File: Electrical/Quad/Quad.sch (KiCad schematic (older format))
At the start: 4 parts, among them J101 01x04, J102 01x04, J103 01x03, J104 01x03

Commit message: Fixed DRC errors
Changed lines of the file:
@@
 $EndComp
 $Comp
-L GND #PWR104
+L GND #PWR01
 U 1 1 5A59574B
 P 9700 1250
-F 0 "#PWR104" H 9700 1000 50  0001 C CNN
+F 0 "#PWR01" H 9700 1000 50  0001 C CNN
 F 1 "GND" H 9700 1100 50  0000 C CNN
 F 2 "" H 9700 1250 50  0001 C CNN
@@
 $EndComp
 $Comp
-L +5V #PWR102
+L +5V #PWR02
 U 1 1 5A595753
 P 9650 1000
-F 0 "#PWR102" H 9650 850 50  0001 C CNN
+F 0 "#PWR02" H 9650 850 50  0001 C CNN
 F 1 "+5V" H 9650 1140 50  0000 C CNN
 F 2 "" H 9650 1000 50  0001 C CNN
@@
 $EndComp
 $Comp
-L GND #PWR105
+L GND #PWR03
 U 1 1 5A59801B
 P 9700 4150
-F 0 "#PWR105" H 9700 3900 50  0001 C CNN
+F 0 "#PWR03" H 9700 3900 50  0001 C CNN
 F 1 "GND" H 9700 4000 50  0000 C CNN
 F 2 "" H 9700 4150 50  0001 C CNN
@@
 $EndComp
 $Comp
-L +5V #PWR103
+L +5V #PWR04
 U 1 1 5A598022
 P 9650 3900
-F 0 "#PWR103" H 9650 3750 50  0001 C CNN
+F 0 "#PWR04" H 9650 3750 50  0001 C CNN
 F 1 "+5V" H 9650 4040 50  0000 C CNN
 F 2 "" H 9650 3900 50  0001 C CNN
@@
 	9700 3900 9650 3900
 $Comp
-L GND #PWR101
+L GND #PWR05
 U 1 1 5A599898
 P 3000 1700
-F 0 "#PWR101" H 3000 1450 50  0001 C CNN
+F 0 "#PWR05" H 3000 1450 50  0001 C CNN
 F 1 "GND" H 3000 1550 50  0000 C CNN
 F 2 "" H 3000 1700 50  0001 C CNN
@@
 	2400 1300 3000 1300
 Wire Wire Line
-	3000 1300 3000 1400
-Wire Wire Line
-	3000 1400 3000 1500
-Wire Wire Line
-	3000 1500 3000 1600
-Wire Wire Line
-	3000 1600 3000 1700
+	3000 1300 3000 1700
 Wire Wire Line
 	2400 1400 3000 1400

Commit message: Added footprints for Quad
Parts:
- J101, J102: footprint (none) -> Pin_Headers:Pin_Header_Straight_1x04_Pitch2.54mm_SMD_Pin1Right
- J103, J104: footprint (none) -> Pin_Headers:Pin_Header_Straight_1x03_Pitch2.54mm_SMD_Pin1Right
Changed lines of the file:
@@
 F 0 "J101" H 9550 2100 50  0000 C CNN
 F 1 "01x04" V 9650 1850 50  0000 C CNN
-F 2 "" H 9550 1900 50  0001 C CNN
+F 2 "Pin_Headers:Pin_Header_Straight_1x04_Pitch2.54mm_SMD_Pin1Right" H 9550 1900 50  0001 C CNN
 F 3 "" H 9550 1900 50  0001 C CNN
 	1    9550 1900
@@
 F 0 "J103" H 9900 1300 50  0000 C CNN
 F 1 "01x03" V 10000 1100 50  0000 C CNN
-F 2 "" H 9900 1100 50  0001 C CNN
+F 2 "Pin_Headers:Pin_Header_Straight_1x03_Pitch2.54mm_SMD_Pin1Right" H 9900 1100 50  0001 C CNN
 F 3 "" H 9900 1100 50  0001 C CNN
 	1    9900 1100
@@
 F 0 "J102" H 9550 5000 50  0000 C CNN
 F 1 "01x04" V 9650 4750 50  0000 C CNN
-F 2 "" H 9550 4800 50  0001 C CNN
+F 2 "Pin_Headers:Pin_Header_Straight_1x04_Pitch2.54mm_SMD_Pin1Right" H 9550 4800 50  0001 C CNN
 F 3 "" H 9550 4800 50  0001 C CNN
 	1    9550 4800
@@
 F 0 "J104" H 9900 4200 50  0000 C CNN
 F 1 "01x03" V 10000 4000 50  0000 C CNN
-F 2 "" H 9900 4000 50  0001 C CNN
+F 2 "Pin_Headers:Pin_Header_Straight_1x03_Pitch2.54mm_SMD_Pin1Right" H 9900 4000 50  0001 C CNN
 F 3 "" H 9900 4000 50  0001 C CNN
 	1    9900 4000

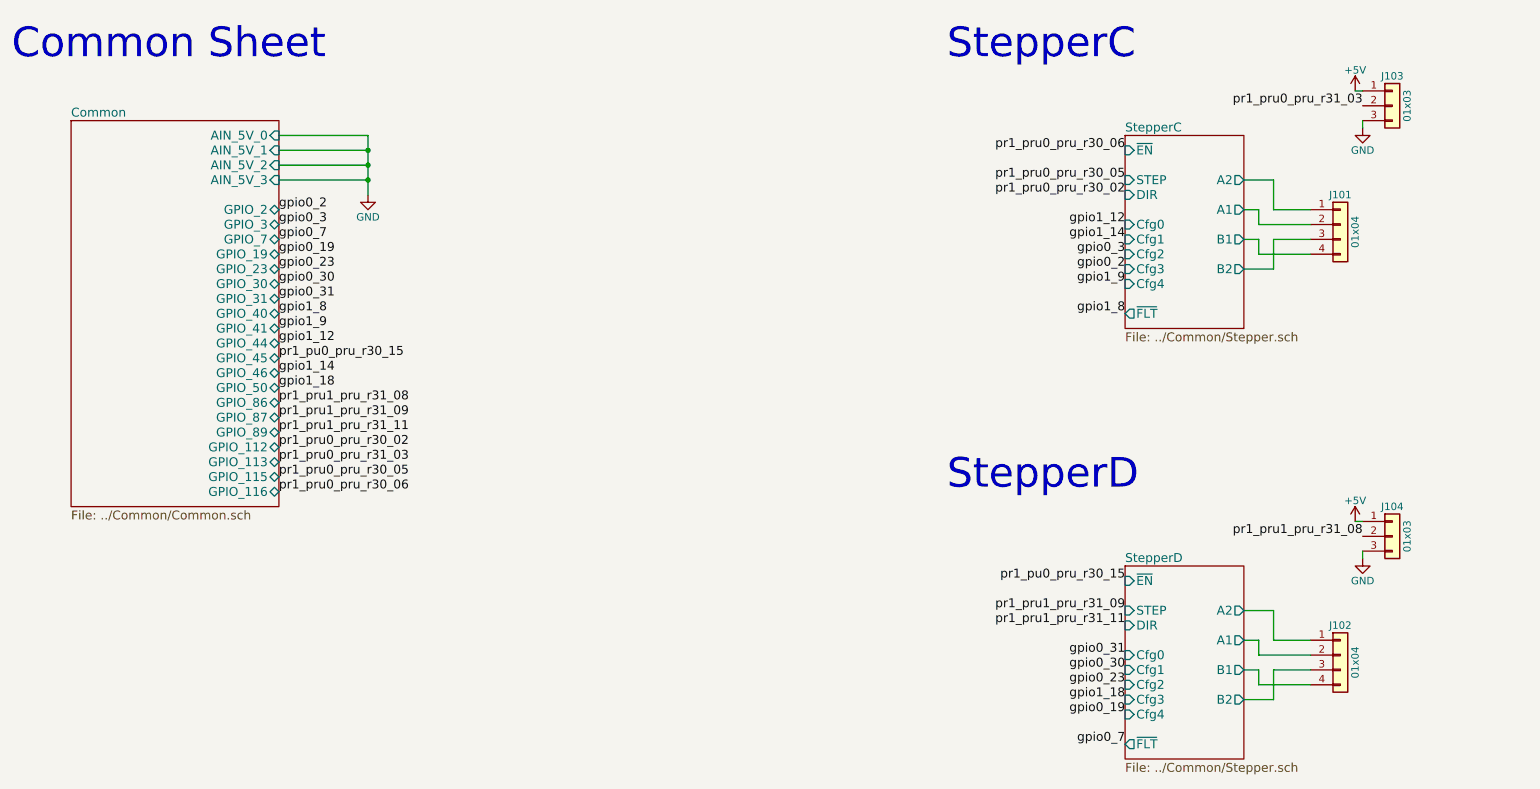
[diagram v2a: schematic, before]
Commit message: Completed Quad stepper version of the board.
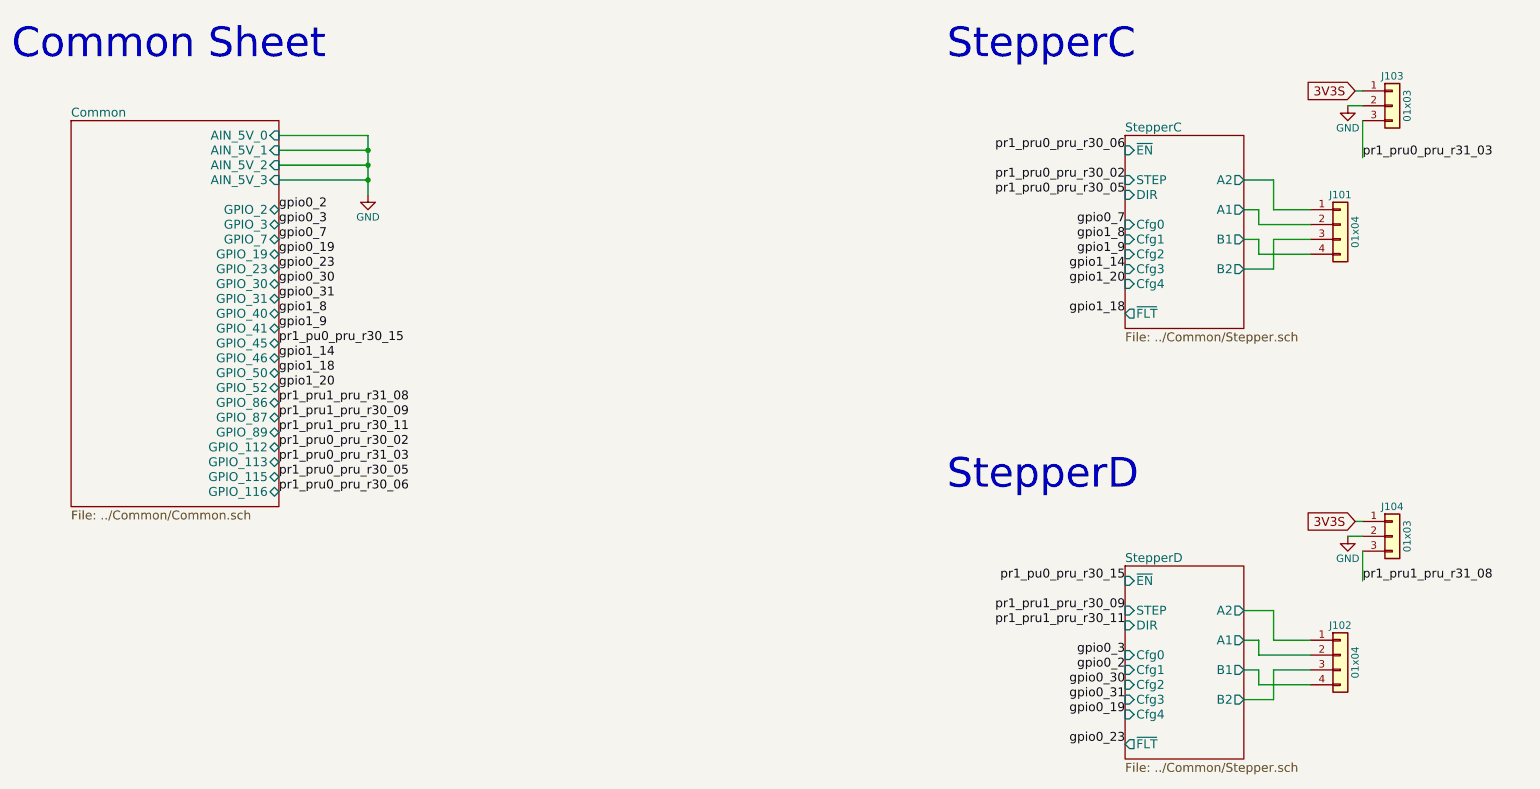
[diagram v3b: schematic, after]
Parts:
- J101, J102: footprint Pin_Headers:Pin_Header_Straight_1x04_Pitch2.54mm_SMD_Pin1Right -> footprints:Molex-SL-4POS
- J103, J104: footprint Pin_Headers:Pin_Header_Straight_1x03_Pitch2.54mm_SMD_Pin1Right -> Connectors_JST:JST_XH_B03B-XH-A_03x2.50mm_Straight
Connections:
- net GND: now also J103.2 (Pin_2), J104.2 (Pin_2); no longer J103.3 (Pin_3), J104.3 (Pin_3)
- net pr1_pru0_pru_r31_03: now also J103.3 (Pin_3); no longer J103.2 (Pin_2)
- net pr1_pru1_pru_r31_08: now also J104.3 (Pin_3); no longer J104.2 (Pin_2)
- net +5V renamed 3V3S
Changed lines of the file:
@@
 LIBS:dc-dc
 LIBS:allegro
+LIBS:mechanical
 LIBS:Quad-cache
 EELAYER 25 0
@@
 F13 "GPIO_40" T R 2400 2500 60
 F14 "GPIO_41" T R 2400 2600 60
-F15 "GPIO_44" T R 2400 2700 60
-F16 "GPIO_45" T R 2400 2800 60
-F17 "GPIO_46" T R 2400 2900 60
-F18 "GPIO_50" T R 2400 3000 60
-F19 "GPIO_86" T R 2400 3100 60
-F20 "GPIO_87" T R 2400 3200 60
-F21 "GPIO_112" T R 2400 3400 60
-F22 "GPIO_113" T R 2400 3500 60
-F23 "GPIO_115" T R 2400 3600 60
-F24 "GPIO_116" T R 2400 3700 60
-F25 "GPIO_89" T R 2400 3300 60
+F15 "GPIO_45" T R 2400 2700 60
+F16 "GPIO_46" T R 2400 2800 60
+F17 "GPIO_50" T R 2400 2900 60
+F18 "GPIO_86" T R 2400 3100 60
+F19 "GPIO_87" T R 2400 3200 60
+F20 "GPIO_112" T R 2400 3400 60
+F21 "GPIO_113" T R 2400 3500 60
+F22 "GPIO_115" T R 2400 3600 60
+F23 "GPIO_116" T R 2400 3700 60
+F24 "GPIO_89" T R 2400 3300 60
+F25 "GPIO_52" T R 2400 3000 60
 $EndSheet
 Text Label 2400 1800 0    60   ~ 0
@@
 Text Label 2400 1900 0    60   ~ 0
 gpio0_3
-Text Label 2400 3000 0    60   ~ 0
+Text Label 2400 2900 0    60   ~ 0
 gpio1_18
 Text Label 2400 2200 0    60   ~ 0
@@
 gpio0_19
 Text Label 2400 2700 0    60   ~ 0
-gpio1_12
+pr1_pu0_pru_r30_15
 Text Label 2400 2800 0    60   ~ 0
-pr1_pu0_pru_r30_15
-Text Label 2400 2900 0    60   ~ 0
 gpio1_14
 Text Label 2400 3100 0    60   ~ 0
 pr1_pru1_pru_r31_08
 Text Label 2400 3200 0    60   ~ 0
-pr1_pru1_pru_r31_09
+pr1_pru1_pru_r30_09
 Text Label 2400 3300 0    60   ~ 0
-pr1_pru1_pru_r31_11
+pr1_pru1_pru_r30_11
 Text Label 2400 3400 0    60   ~ 0
 pr1_pru0_pru_r30_02
@@
 U 1 1 5A595731
 P 9550 1900
+AR Path="/5A595731" Ref="J101"  Part="1"
+AR Path="/5A579457/5A595731" Ref="J101"  Part="1"
 F 0 "J101" H 9550 2100 50  0000 C CNN
 F 1 "01x04" V 9650 1850 50  0000 C CNN
-F 2 "Pin_Headers:Pin_Header_Straight_1x04_Pitch2.54mm_SMD_Pin1Right" H 9550 1900 50  0001 C CNN
+F 2 "footprints:Molex-SL-4POS" H 9550 1900 50  0001 C CNN
 F 3 "" H 9550 1900 50  0001 C CNN
 	1    9550 1900
@@
 F 0 "J103" H 9900 1300 50  0000 C CNN
 F 1 "01x03" V 10000 1100 50  0000 C CNN
-F 2 "Pin_Headers:Pin_Header_Straight_1x03_Pitch2.54mm_SMD_Pin1Right" H 9900 1100 50  0001 C CNN
+F 2 "Connectors_JST:JST_XH_B03B-XH-A_03x2.50mm_Straight" H 9900 1100 50  0001 C CNN
 F 3 "" H 9900 1100 50  0001 C CNN
 	1    9900 1100
-	1    0    0    -1
-$EndComp
-$Comp
-L GND #PWR01
-U 1 1 5A59574B
-P 9700 1250
-F 0 "#PWR01" H 9700 1000 50  0001 C CNN
-F 1 "GND" H 9700 1100 50  0000 C CNN
-F 2 "" H 9700 1250 50  0001 C CNN
-F 3 "" H 9700 1250 50  0001 C CNN
-	1    9700 1250
-	-1   0    0    -1
-$EndComp
-$Comp
-L +5V #PWR02
-U 1 1 5A595753
-P 9650 1000
-F 0 "#PWR02" H 9650 850 50  0001 C CNN
-F 1 "+5V" H 9650 1140 50  0000 C CNN
-F 2 "" H 9650 1000 50  0001 C CNN
-F 3 "" H 9650 1000 50  0001 C CNN
-	1    9650 1000
 	1    0    0    -1
 $EndComp
@@
 F 0 "J102" H 9550 5000 50  0000 C CNN
 F 1 "01x04" V 9650 4750 50  0000 C CNN
-F 2 "Pin_Headers:Pin_Header_Straight_1x04_Pitch2.54mm_SMD_Pin1Right" H 9550 4800 50  0001 C CNN
+F 2 "footprints:Molex-SL-4POS" H 9550 4800 50  0001 C CNN
 F 3 "" H 9550 4800 50  0001 C CNN
 	1    9550 4800
@@
 F 0 "J104" H 9900 4200 50  0000 C CNN
 F 1 "01x03" V 10000 4000 50  0000 C CNN
-F 2 "Pin_Headers:Pin_Header_Straight_1x03_Pitch2.54mm_SMD_Pin1Right" H 9900 4000 50  0001 C CNN
+F 2 "Connectors_JST:JST_XH_B03B-XH-A_03x2.50mm_Straight" H 9900 4000 50  0001 C CNN
 F 3 "" H 9900 4000 50  0001 C CNN
 	1    9900 4000
@@
 $EndComp
 $Comp
-L GND #PWR03
+L GND #PWR01
 U 1 1 5A59801B
-P 9700 4150
-F 0 "#PWR03" H 9700 3900 50  0001 C CNN
-F 1 "GND" H 9700 4000 50  0000 C CNN
-F 2 "" H 9700 4150 50  0001 C CNN
-F 3 "" H 9700 4150 50  0001 C CNN
-	1    9700 4150
+P 9600 4000
+F 0 "#PWR01" H 9600 3750 50  0001 C CNN
+F 1 "GND" H 9600 3850 50  0000 C CNN
+F 2 "" H 9600 4000 50  0001 C CNN
+F 3 "" H 9600 4000 50  0001 C CNN
+	1    9600 4000
 	-1   0    0    -1
 $EndComp
-$Comp
-L +5V #PWR04
-U 1 1 5A598022
-P 9650 3900
-F 0 "#PWR04" H 9650 3750 50  0001 C CNN
-F 1 "+5V" H 9650 4040 50  0000 C CNN
-F 2 "" H 9650 3900 50  0001 C CNN
-F 3 "" H 9650 3900 50  0001 C CNN
-	1    9650 3900
-	1    0    0    -1
-$EndComp
 Wire Wire Line
 	8900 1600 9100 1600
@@
 	9100 2000 9350 2000
 Wire Wire Line
-	9700 1250 9700 1200
-Wire Wire Line
 	9700 1000 9650 1000
 Wire Wire Line
@@
 	9100 4900 9350 4900
 Wire Wire Line
-	9700 4150 9700 4100
-Wire Wire Line
 	9700 3900 9650 3900
 $Comp
-L GND #PWR05
+L GND #PWR02
 U 1 1 5A599898
 P 3000 1700
-F 0 "#PWR05" H 3000 1450 50  0001 C CNN
+F 0 "#PWR02" H 3000 1450 50  0001 C CNN
 F 1 "GND" H 3000 1550 50  0000 C CNN
 F 2 "" H 3000 1700 50  0001 C CNN
@@
 	2400 1600 3000 1600
 Connection ~ 3000 1600
+Text Label 8100 1600 2    60   ~ 0
+pr1_pru0_pru_r30_02
 Text Label 8100 1700 2    60   ~ 0
-pr1_pru0_pru_r30_02
-Text Label 8100 1600 2    60   ~ 0
 pr1_pru0_pru_r30_05
+Text Label 8100 4900 2    60   ~ 0
+gpio0_2
+Text Label 8100 4800 2    60   ~ 0
+gpio0_3
 Text Label 8100 2200 2    60   ~ 0
-gpio0_2
-Text Label 8100 2100 2    60   ~ 0
-gpio0_3
-Text Label 8100 2000 2    60   ~ 0
 gpio1_14
-Text Label 8100 1900 2    60   ~ 0
-gpio1_12
 Text Label 8100 1400 2    60   ~ 0
 pr1_pru0_pru_r30_06
-Text Label 8100 2500 2    60   ~ 0
+Text Label 8100 2000 2    60   ~ 0
 gpio1_8
-Text Label 8100 2300 2    60   ~ 0
+Text Label 8100 2100 2    60   ~ 0
 gpio1_9
-Text Label 9700 1100 2    60   ~ 0
-pr1_pru0_pru_r31_03
-Text Label 9700 4000 2    60   ~ 0
+Text Label 9700 4300 0    60   ~ 0
 pr1_pru1_pru_r31_08
 Text Label 8100 4600 2    60   ~ 0
-pr1_pru1_pru_r31_11
+pr1_pru1_pru_r30_11
 Text Label 8100 4500 2    60   ~ 0
-pr1_pru1_pru_r31_09
+pr1_pru1_pru_r30_09
+Text Label 8100 2500 2    60   ~ 0
+gpio1_18
+Text Label 8100 5400 2    60   ~ 0
+gpio0_23
+Text Label 8100 5000 2    60   ~ 0
+gpio0_30
 Text Label 8100 5100 2    60   ~ 0
-gpio1_18
-Text Label 8100 5000 2    60   ~ 0
-gpio0_23
-Text Label 8100 4900 2    60   ~ 0
-gpio0_30
-Text Label 8100 4800 2    60   ~ 0
 gpio0_31
 Text Label 8100 4300 2    60   ~ 0
 pr1_pu0_pru_r30_15
-Text Label 8100 5400 2    60   ~ 0
+Text Label 8100 1900 2    60   ~ 0
 gpio0_7
 Text Label 8100 5200 2    60   ~ 0
 gpio0_19
+Text Label 2400 3000 0    60   ~ 0
+gpio1_20
+Text Label 8100 2300 2    60   ~ 0
+gpio1_20
+Wire Wire Line
+	9700 4000 9600 4000
+Wire Wire Line
+	9700 4100 9700 4300
+Text Label 9700 1450 0    60   ~ 0
+pr1_pru0_pru_r31_03
+Wire Wire Line
+	9700 1200 9700 1450
+$Comp
+L GND #PWR03
+U 1 1 5A618A31
+P 9600 1100
+F 0 "#PWR03" H 9600 850 50  0001 C CNN
+F 1 "GND" H 9600 950 50  0000 C CNN
+F 2 "" H 9600 1100 50  0001 C CNN
+F 3 "" H 9600 1100 50  0001 C CNN
+	1    9600 1100
+	-1   0    0    -1
+$EndComp
+Wire Wire Line
+	9700 1100 9600 1100
+Text GLabel 9650 1000 0    60   Input ~ 0
+3V3S
+Text GLabel 9650 3900 0    60   Input ~ 0
+3V3S
 $EndSCHEMATC
